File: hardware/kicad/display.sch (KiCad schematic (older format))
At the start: 6 parts, among them U7 ER-TFT040-2

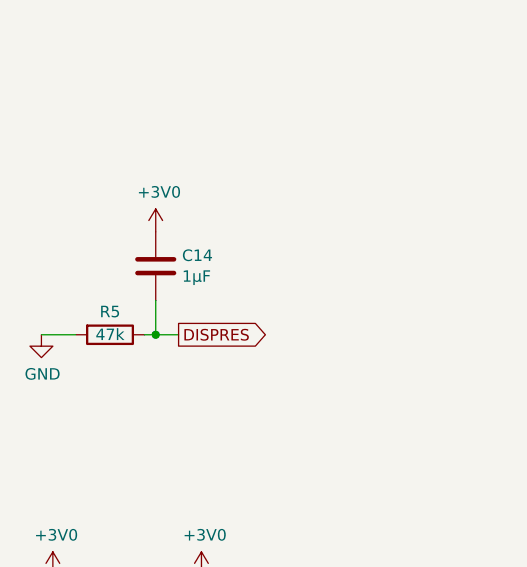
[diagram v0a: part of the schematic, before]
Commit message: Rework display reset circuit and improve 3v power supply
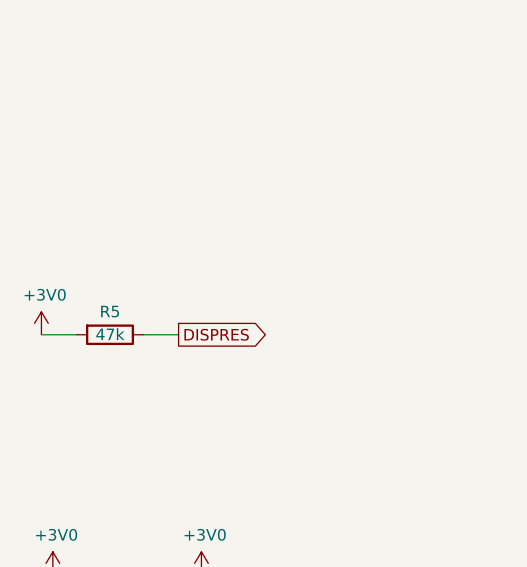
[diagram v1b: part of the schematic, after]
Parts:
- removed C14: 1µF, Capacitor_SMD:C_0603_1608Metric, symbol Device:C
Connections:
- net +3V0: now also R5.2
- net GND: no longer R5.2
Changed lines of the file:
@@
 	0    1    1    0
 $EndComp
-Wire Wire Line
-	3000 3100 3050 3100
 Text GLabel 3150 3100 2    50   Output ~ 0
 DISPRES
 Wire Wire Line
 	2700 3100 2550 3100
-$Comp
-L power:GND #PWR055
-U 1 1 5F0AE40B
-P 2550 3100
-F 0 "#PWR055" H 2550 2850 50  0001 C CNN
-F 1 "GND" H 2555 2927 50  0000 C CNN
-F 2 "" H 2550 3100 50  0001 C CNN
-F 3 "" H 2550 3100 50  0001 C CNN
-	1    2550 3100
-	1    0    0    -1
-$EndComp
-$Comp
-L Device:C C14
-U 1 1 5F0AE8D8
-P 3050 2800
-F 0 "C14" H 3165 2846 50  0000 L CNN
-F 1 "1µF" H 3165 2755 50  0000 L CNN
-F 2 "Capacitor_SMD:C_0603_1608Metric" H 3088 2650 50  0001 C CNN
-F 3 "~" H 3050 2800 50  0001 C CNN
-F 4 "C15849" H 3050 2800 50  0001 C CNN "LCSC"
-	1    3050 2800
-	1    0    0    -1
-$EndComp
-Wire Wire Line
-	3050 2950 3050 3100
-Connection ~ 3050 3100
-Wire Wire Line
-	3050 3100 3150 3100
-$Comp
-L power:+3V0 #PWR054
-U 1 1 5F0AF94A
-P 3050 2650
-F 0 "#PWR054" H 3050 2500 50  0001 C CNN
-F 1 "+3V0" H 3065 2823 50  0000 C CNN
-F 2 "" H 3050 2650 50  0001 C CNN
-F 3 "" H 3050 2650 50  0001 C CNN
-	1    3050 2650
-	1    0    0    -1
-$EndComp
 Text GLabel 5600 3400 0    50   Input ~ 0
 B0
@@
 	1    0    0    -1
 $EndComp
+Wire Wire Line
+	3000 3100 3150 3100
+$Comp
+L power:+3V0 #PWR?
+U 1 1 5F132328
+P 2550 3100
+F 0 "#PWR?" H 2550 2950 50  0001 C CNN
+F 1 "+3V0" H 2565 3273 50  0000 C CNN
+F 2 "" H 2550 3100 50  0001 C CNN
+F 3 "" H 2550 3100 50  0001 C CNN
+	1    2550 3100
+	1    0    0    -1
+$EndComp

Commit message: Add digikey bom alternative
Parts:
- C15, C16: DigiKey (none) -> 311-1335-1-ND
- R4: DigiKey (none) -> 311-100HRCT-ND
- R5: DigiKey (none) -> 311-47KGRCT-ND
- U7: DigiKey (none) -> HFV160CT-ND
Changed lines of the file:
@@
 F 2 "Connector_FFC-FPC:TE_5-1734839-0_1x60-1MP_P0.5mm_Horizontal_HandSolder" H 5750 6100 50  0001 C CNN
 F 3 "" H 5750 6100 50  0001 C CNN
+F 4 "HFV160CT-ND" H 5850 4100 50  0001 C CNN "DigiKey"
 	1    5850 4100
 	1    0    0    -1
@@
 F 3 "~" H 5100 1100 50  0001 C CNN
 F 4 "C22775" H 5100 1100 50  0001 C CNN "LCSC"
+F 5 "311-100HRCT-ND" H 5100 1100 50  0001 C CNN "DigiKey"
 	1    5100 1100
 	0    1    1    0
@@
 F 3 "~" H 2850 3100 50  0001 C CNN
 F 4 "C25819 " H 2850 3100 50  0001 C CNN "LCSC"
+F 5 "311-47KGRCT-ND" H 2850 3100 50  0001 C CNN "DigiKey"
 	1    2850 3100
 	0    1    1    0
@@
 F 3 "~" H 2600 4300 50  0001 C CNN
 F 4 "C14663" H 2600 4300 50  0001 C CNN "LCSC"
+F 5 "311-1335-1-ND" H 2600 4300 50  0001 C CNN "DigiKey"
 	1    2600 4300
 	1    0    0    -1
@@
 F 3 "~" H 3250 4300 50  0001 C CNN
 F 4 "C14663" H 3250 4300 50  0001 C CNN "LCSC"
+F 5 "311-1335-1-ND" H 3250 4300 50  0001 C CNN "DigiKey"
 	1    3250 4300
 	1    0    0    -1

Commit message: Update footprints for machine assembly
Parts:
- U7: footprint Connector_FFC-FPC:TE_5-1734839-0_1x60-1MP_P0.5mm_Horizontal_HandSolder -> kicad:HRS_FH28-60S-0.5SH(05)
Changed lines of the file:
@@
 F 0 "U7" H 6078 4201 50  0000 L CNN
 F 1 "ER-TFT040-2" H 6078 4110 50  0000 L CNN
-F 2 "Connector_FFC-FPC:TE_5-1734839-0_1x60-1MP_P0.5mm_Horizontal_HandSolder" H 5750 6100 50  0001 C CNN
+F 2 "kicad:HRS_FH28-60S-0.5SH(05)" H 5750 6100 50  0001 C CNN
 F 3 "" H 5750 6100 50  0001 C CNN
 F 4 "HFV160CT-ND" H 5850 4100 50  0001 C CNN "DigiKey"

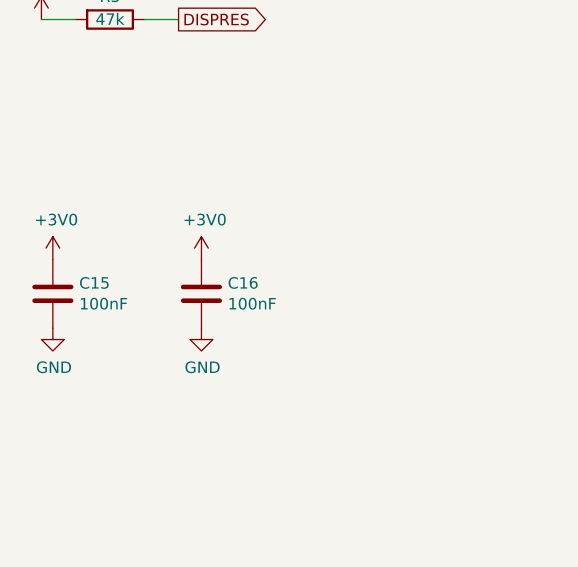
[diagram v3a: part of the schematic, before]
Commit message: Clean up board and expose less debug signals
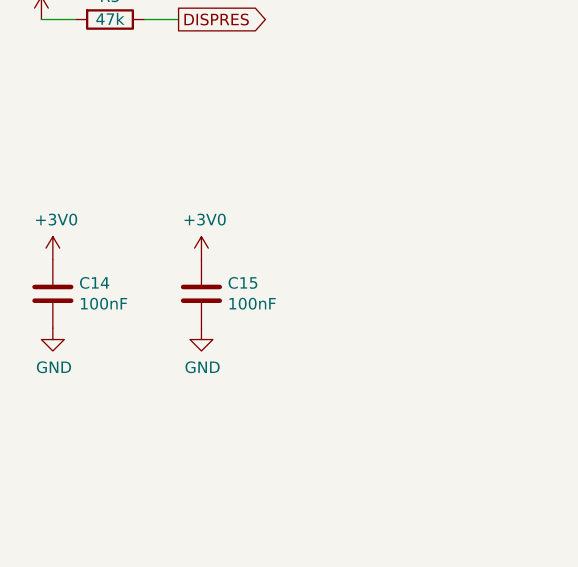
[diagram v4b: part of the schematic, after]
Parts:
- renumbered C15 to C14, C16 to C15
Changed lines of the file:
@@
 $EndDescr
 $Comp
-L driver-board-rescue:ER-TFT040-2-driver-board-driver-board-rescue U7
+L driver-board-rescue:ER-TFT040-2-driver-board-driver-board-rescue U?
 U 1 1 5F09E273
 P 5850 4100
-AR Path="/5F09E273" Ref="U7"  Part="1"
+AR Path="/5F09E273" Ref="U?"  Part="1"
 AR Path="/5F096907/5F09E273" Ref="U7"  Part="1"
 F 0 "U7" H 6078 4201 50  0000 L CNN
@@
 	5600 1100 5250 1100
 $Comp
-L power:+12V #PWR050
+L power:+12V #PWR052
 U 1 1 5F0A5C59
 P 4950 1100
-F 0 "#PWR050" H 4950 950 50  0001 C CNN
+F 0 "#PWR052" H 4950 950 50  0001 C CNN
 F 1 "+12V" V 4950 1200 50  0000 L CNN
 F 2 "" H 4950 1100 50  0001 C CNN
@@
 	5450 2200 5450 2300
 $Comp
-L power:GND #PWR053
+L power:GND #PWR055
 U 1 1 5F0A863D
 P 5450 2100
-F 0 "#PWR053" H 5450 1850 50  0001 C CNN
+F 0 "#PWR055" H 5450 1850 50  0001 C CNN
 F 1 "GND" V 5450 2000 50  0000 R CNN
 F 2 "" H 5450 2100 50  0001 C CNN
@@
 DE
 $Comp
-L power:GND #PWR056
+L power:GND #PWR057
 U 1 1 5F0A8F83
 P 5600 3300
-F 0 "#PWR056" H 5600 3050 50  0001 C CNN
+F 0 "#PWR057" H 5600 3050 50  0001 C CNN
 F 1 "GND" V 5600 3200 50  0000 R CNN
 F 2 "" H 5600 3300 50  0001 C CNN
@@
 SDI_3V
 $Comp
-L power:GND #PWR052
+L power:GND #PWR054
 U 1 1 5F0AA3B1
 P 5600 1400
-F 0 "#PWR052" H 5600 1150 50  0001 C CNN
+F 0 "#PWR054" H 5600 1150 50  0001 C CNN
 F 1 "GND" V 5600 1300 50  0000 R CNN
 F 2 "" H 5600 1400 50  0001 C CNN
@@
 $EndComp
 $Comp
-L power:GND #PWR051
+L power:GND #PWR053
 U 1 1 5F0AA4C0
 P 5450 1200
-F 0 "#PWR051" H 5450 950 50  0001 C CNN
+F 0 "#PWR053" H 5450 950 50  0001 C CNN
 F 1 "GND" V 5450 1100 50  0000 R CNN
 F 2 "" H 5450 1200 50  0001 C CNN
@@
 Connection ~ 5450 1200
 $Comp
-L power:+3V0 #PWR066
+L power:+3V0 #PWR067
 U 1 1 5F0AACF6
 P 5600 7000
-F 0 "#PWR066" H 5600 6850 50  0001 C CNN
+F 0 "#PWR067" H 5600 6850 50  0001 C CNN
 F 1 "+3V0" V 5600 7100 50  0000 L CNN
 F 2 "" H 5600 7000 50  0001 C CNN
@@
 $EndComp
 $Comp
-L power:+3V0 #PWR065
+L power:+3V0 #PWR066
 U 1 1 5F0AAE66
 P 5600 6900
-F 0 "#PWR065" H 5600 6750 50  0001 C CNN
+F 0 "#PWR066" H 5600 6750 50  0001 C CNN
 F 1 "+3V0" V 5600 7000 50  0000 L CNN
 F 2 "" H 5600 6900 50  0001 C CNN
@@
 $EndComp
 $Comp
-L power:+3V0 #PWR064
+L power:+3V0 #PWR065
 U 1 1 5F0AB3E3
 P 5600 6800
-F 0 "#PWR064" H 5600 6650 50  0001 C CNN
+F 0 "#PWR065" H 5600 6650 50  0001 C CNN
 F 1 "+3V0" V 5600 6900 50  0000 L CNN
 F 2 "" H 5600 6800 50  0001 C CNN
@@
 $EndComp
 $Comp
-L power:+3V0 #PWR061
+L power:+3V0 #PWR062
 U 1 1 5F0AB772
 P 5600 6500
-F 0 "#PWR061" H 5600 6350 50  0001 C CNN
+F 0 "#PWR062" H 5600 6350 50  0001 C CNN
 F 1 "+3V0" V 5600 6600 50  0000 L CNN
 F 2 "" H 5600 6500 50  0001 C CNN
@@
 $EndComp
 $Comp
-L power:GND #PWR062
+L power:GND #PWR063
 U 1 1 5F0ABD62
 P 5600 6600
-F 0 "#PWR062" H 5600 6350 50  0001 C CNN
+F 0 "#PWR063" H 5600 6350 50  0001 C CNN
 F 1 "GND" V 5600 6500 50  0000 R CNN
 F 2 "" H 5600 6600 50  0001 C CNN
@@
 $EndComp
 $Comp
-L power:GND #PWR063
+L power:GND #PWR064
 U 1 1 5F0AC4D7
 P 5600 6700
-F 0 "#PWR063" H 5600 6450 50  0001 C CNN
+F 0 "#PWR064" H 5600 6450 50  0001 C CNN
 F 1 "GND" V 5600 6600 50  0000 R CNN
 F 2 "" H 5600 6700 50  0001 C CNN
@@
 R7
 $Comp
-L Device:C C15
+L Device:C C14
 U 1 1 5F0D003B
 P 2600 4300
-F 0 "C15" H 2715 4346 50  0000 L CNN
+F 0 "C14" H 2715 4346 50  0000 L CNN
 F 1 "100nF" H 2715 4255 50  0000 L CNN
 F 2 "Capacitor_SMD:C_0603_1608Metric" H 2638 4150 50  0001 C CNN
@@
 $EndComp
 $Comp
-L power:+3V0 #PWR057
+L power:+3V0 #PWR058
 U 1 1 5F0D0D40
 P 2600 4150
-F 0 "#PWR057" H 2600 4000 50  0001 C CNN
+F 0 "#PWR058" H 2600 4000 50  0001 C CNN
 F 1 "+3V0" H 2615 4323 50  0000 C CNN
 F 2 "" H 2600 4150 50  0001 C CNN
@@
 $EndComp
 $Comp
-L power:GND #PWR059
+L power:GND #PWR060
 U 1 1 5F0D1567
 P 2600 4450
-F 0 "#PWR059" H 2600 4200 50  0001 C CNN
+F 0 "#PWR060" H 2600 4200 50  0001 C CNN
 F 1 "GND" H 2605 4277 50  0000 C CNN
 F 2 "" H 2600 4450 50  0001 C CNN
@@
 $EndComp
 $Comp
-L Device:C C16
+L Device:C C15
 U 1 1 5F0D6490
 P 3250 4300
-F 0 "C16" H 3365 4346 50  0000 L CNN
+F 0 "C15" H 3365 4346 50  0000 L CNN
 F 1 "100nF" H 3365 4255 50  0000 L CNN
 F 2 "Capacitor_SMD:C_0603_1608Metric" H 3288 4150 50  0001 C CNN
@@
 $EndComp
 $Comp
-L power:+3V0 #PWR058
+L power:+3V0 #PWR059
 U 1 1 5F0D6496
 P 3250 4150
-F 0 "#PWR058" H 3250 4000 50  0001 C CNN
+F 0 "#PWR059" H 3250 4000 50  0001 C CNN
 F 1 "+3V0" H 3265 4323 50  0000 C CNN
 F 2 "" H 3250 4150 50  0001 C CNN
@@
 $EndComp
 $Comp
-L power:GND #PWR060
+L power:GND #PWR061
 U 1 1 5F0D649C
 P 3250 4450
-F 0 "#PWR060" H 3250 4200 50  0001 C CNN
+F 0 "#PWR061" H 3250 4200 50  0001 C CNN
 F 1 "GND" H 3255 4277 50  0000 C CNN
 F 2 "" H 3250 4450 50  0001 C CNN
@@
 	3000 3100 3150 3100
 $Comp
-L power:+3V0 #PWR?
+L power:+3V0 #PWR056
 U 1 1 5F132328
 P 2550 3100
-F 0 "#PWR?" H 2550 2950 50  0001 C CNN
+F 0 "#PWR056" H 2550 2950 50  0001 C CNN
 F 1 "+3V0" H 2565 3273 50  0000 C CNN
 F 2 "" H 2550 3100 50  0001 C CNN

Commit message: Update BOM
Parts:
- C14, C15: Description (none) -> CAP CER 0.1UF 16V X7R 0603; DigiKey 311-1335-1-ND -> (none); Manufacturer (none) -> Yageo; Mfg Part # (none) -> CC0603KPX7R7BB104
- R4: Description (none) -> RES SMD 100 OHM 1% 1/10W 0603; DigiKey 311-100HRCT-ND -> (none); Manufacturer (none) -> Yageo; Mfg Part # (none) -> RC0603FR-07100RL
- R5: Description (none) -> RES SMD 47K OHM 5% 1/10W 0603; DigiKey 311-47KGRCT-ND -> (none); Manufacturer (none) -> Yageo; Mfg Part # (none) -> RC0603JR-0747KL
- U7: Description (none) -> CONN FFC BOTTOM 60POS 0.50MM R/A; DigiKey HFV160CT-ND -> (none); Manufacturer (none) -> Hirose Electric Co Ltd; Mfg Part # (none) -> FH28-60S-0.5SH(05)
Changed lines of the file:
@@
 F 2 "kicad:HRS_FH28-60S-0.5SH(05)" H 5750 6100 50  0001 C CNN
 F 3 "" H 5750 6100 50  0001 C CNN
-F 4 "HFV160CT-ND" H 5850 4100 50  0001 C CNN "DigiKey"
+F 4 "" H 5850 4100 50  0001 C CNN "DigiKey"
+F 5 "FH28-60S-0.5SH(05)" H 5850 4100 50  0001 C CNN "Mfg Part #"
+F 6 "CONN FFC BOTTOM 60POS 0.50MM R/A" H 5850 4100 50  0001 C CNN "Description"
+F 7 "Hirose Electric Co Ltd" H 5850 4100 50  0001 C CNN "Manufacturer"
 	1    5850 4100
 	1    0    0    -1
@@
 F 3 "~" H 5100 1100 50  0001 C CNN
 F 4 "C22775" H 5100 1100 50  0001 C CNN "LCSC"
-F 5 "311-100HRCT-ND" H 5100 1100 50  0001 C CNN "DigiKey"
+F 5 "" H 5100 1100 50  0001 C CNN "DigiKey"
+F 6 "RC0603FR-07100RL" H 5100 1100 50  0001 C CNN "Mfg Part #"
+F 7 "RES SMD 100 OHM 1% 1/10W 0603" H 5100 1100 50  0001 C CNN "Description"
+F 8 "Yageo" H 5100 1100 50  0001 C CNN "Manufacturer"
 	1    5100 1100
 	0    1    1    0
@@
 F 3 "~" H 2850 3100 50  0001 C CNN
 F 4 "C25819 " H 2850 3100 50  0001 C CNN "LCSC"
-F 5 "311-47KGRCT-ND" H 2850 3100 50  0001 C CNN "DigiKey"
+F 5 "" H 2850 3100 50  0001 C CNN "DigiKey"
+F 6 "RC0603JR-0747KL" H 2850 3100 50  0001 C CNN "Mfg Part #"
+F 7 "RES SMD 47K OHM 5% 1/10W 0603" H 2850 3100 50  0001 C CNN "Description"
+F 8 "Yageo" H 2850 3100 50  0001 C CNN "Manufacturer"
 	1    2850 3100
 	0    1    1    0
@@
 F 3 "~" H 2600 4300 50  0001 C CNN
 F 4 "C14663" H 2600 4300 50  0001 C CNN "LCSC"
-F 5 "311-1335-1-ND" H 2600 4300 50  0001 C CNN "DigiKey"
+F 5 "" H 2600 4300 50  0001 C CNN "DigiKey"
+F 6 "CC0603KPX7R7BB104" H 2600 4300 50  0001 C CNN "Mfg Part #"
+F 7 "CAP CER 0.1UF 16V X7R 0603" H 2600 4300 50  0001 C CNN "Description"
+F 8 "Yageo" H 2600 4300 50  0001 C CNN "Manufacturer"
 	1    2600 4300
 	1    0    0    -1
@@
 F 3 "~" H 3250 4300 50  0001 C CNN
 F 4 "C14663" H 3250 4300 50  0001 C CNN "LCSC"
-F 5 "311-1335-1-ND" H 3250 4300 50  0001 C CNN "DigiKey"
+F 5 "" H 3250 4300 50  0001 C CNN "DigiKey"
+F 6 "CC0603KPX7R7BB104" H 3250 4300 50  0001 C CNN "Mfg Part #"
+F 7 "CAP CER 0.1UF 16V X7R 0603" H 3250 4300 50  0001 C CNN "Description"
+F 8 "Yageo" H 3250 4300 50  0001 C CNN "Manufacturer"
 	1    3250 4300
 	1    0    0    -1
